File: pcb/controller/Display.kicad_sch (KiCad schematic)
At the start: 24 parts, among them J10 JST XH, J11 JST XH, J12 JST XH, J13 JST XH, J5 OLED 0.96" (I2C), J6 JST XH, J7 JST XH, J8 JST XH, J9 JST XH, Q2 SI2301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

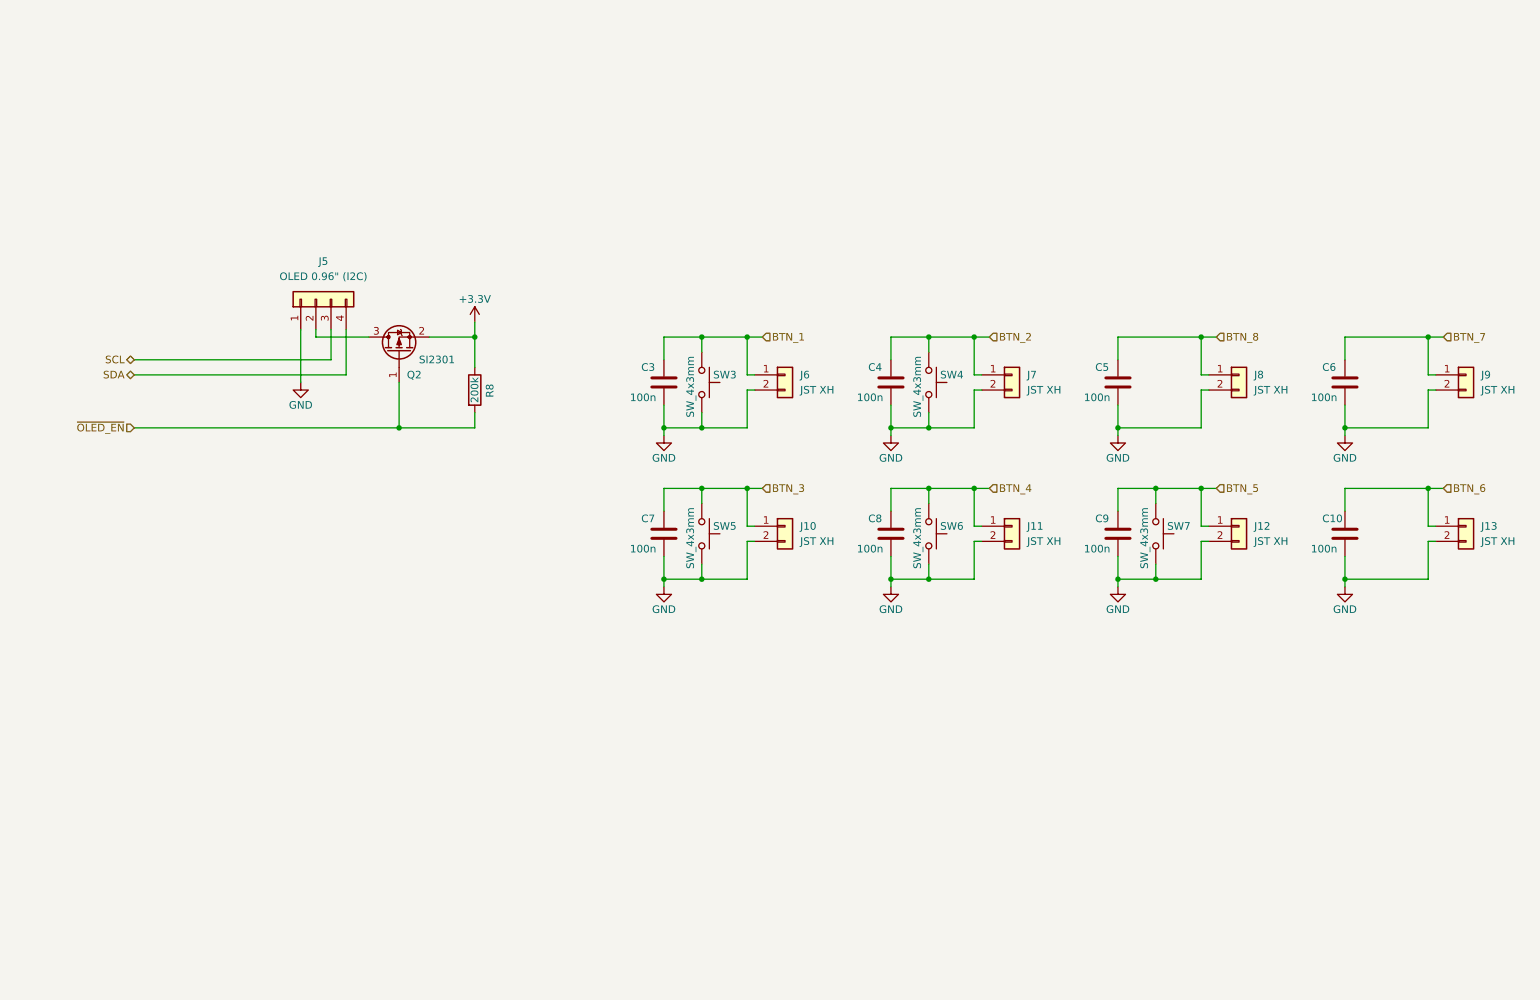
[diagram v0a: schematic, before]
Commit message: Revision 01 of Controller hardware
- fixed bugs from revision 00
- changed folder structure
- added ReleaseNotes_Controller.md to keep track of changes
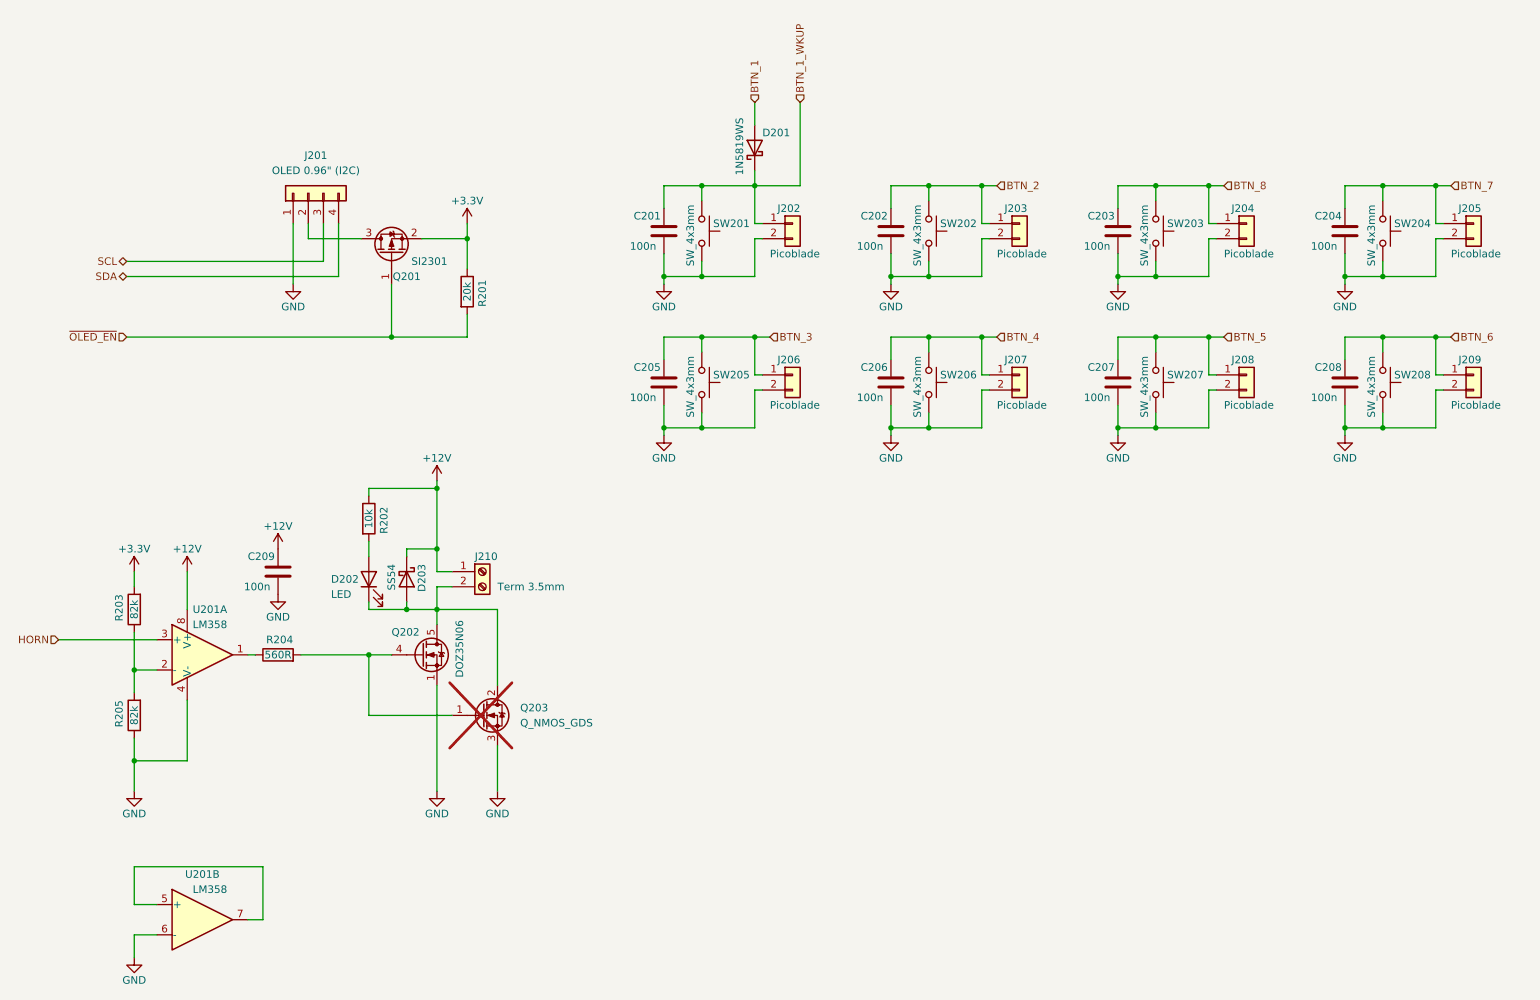
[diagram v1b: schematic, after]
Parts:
- added C209: 100n, Capacitor_SMD:C_0402_1005Metric, symbol Device:C
- added D201: 1N5819WS, Diode_SMD:D_SOD-323, symbol Diode:1N5819WS
- added D202: LED, LED_SMD:LED_0603_1608Metric, symbol Device:LED
- added D203: SS54, Diode_SMD:D_SMA, symbol Device:D_Schottky
- added J210: Term 3.5mm, Connector_Phoenix_MC:PhoenixContact_MC_1,5_2-G-3.5_1x02_P3.50mm_Horizontal, symbol Connector:Screw_Terminal_01x02
- added Q202: DOZ35N06, Package_SON:VSON-8_3.3x3.3mm_P0.65mm_NexFET, symbol Ravenspark:60N03D
- added Q203: Q_NMOS_GDS, Package_TO_SOT_SMD:TO-252-2, symbol Device:Q_NMOS_GDS
- added R202: 10k, Resistor_SMD:R_0402_1005Metric, symbol Device:R
- added R203, R205: 82k, Resistor_SMD:R_0402_1005Metric, symbol Device:R
- added R204: 560R, Resistor_SMD:R_0402_1005Metric, symbol Device:R
- added SW203, SW204, SW208: SW_4x3mm, RVNSPRK_Switch:SW_Push_4x3mm, symbol Switch:SW_Push
- added U201: LM358, Package_SO:SOIC-8_3.9x4.9mm_P1.27mm, symbol Amplifier_Operational:LM358
- C201: renamed from C3; LCSC Part # (none) -> C307331
- C202: renamed from C4; LCSC Part # (none) -> C307331
- C203: renamed from C5; LCSC Part # (none) -> C307331
- C204: renamed from C6; LCSC Part # (none) -> C307331
- C205: renamed from C7; LCSC Part # (none) -> C307331
- C206: renamed from C8; LCSC Part # (none) -> C307331
- C207: renamed from C9; LCSC Part # (none) -> C307331
- C208: renamed from C10; LCSC Part # (none) -> C307331
- J201: renamed from J5; footprint Connector_PinSocket_2.54mm:PinSocket_1x04_P2.54mm_Vertical -> Connector_PinSocket_2.54mm:PinSocket_1x04_P2.54mm_Vertical_SMD_Pin1Left; LCSC Part # (none) -> C20071191
- J202: renamed from J6; value JST XH -> Picoblade; LCSC Part # (none) -> C2845535
- J203: renamed from J7; value JST XH -> Picoblade; LCSC Part # (none) -> C2845535
- J204: renamed from J8; value JST XH -> Picoblade; LCSC Part # (none) -> C2845535
- J205: renamed from J9; value JST XH -> Picoblade; LCSC Part # (none) -> C2845535
- J206: renamed from J10; value JST XH -> Picoblade; LCSC Part # (none) -> C2845535
- J207: renamed from J11; value JST XH -> Picoblade; LCSC Part # (none) -> C2845535
- J208: renamed from J12; value JST XH -> Picoblade; LCSC Part # (none) -> C2845535
- J209: renamed from J13; value JST XH -> Picoblade; LCSC Part # (none) -> C2845535
- Q201: renamed from Q2; LCSC Part # (none) -> C10487
- R201: renamed from R8; value 200k -> 20k
- SW201: renamed from SW3; LCSC Part # (none) -> C18078117
- SW202: renamed from SW4; LCSC Part # (none) -> C18078117
- SW205: renamed from SW5; LCSC Part # (none) -> C18078117
- SW206: renamed from SW6; LCSC Part # (none) -> C18078117
- SW207: renamed from SW7; LCSC Part # (none) -> C18078117
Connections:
- net +3.3V: now also R203.2
- net BTN_1: now also D201.2 (A); no longer C201.1, J202.1 (Pin_1), SW201.1
- net BTN_6: now also SW208.1
- net BTN_7: now also SW204.1
- net BTN_8: now also SW203.1
- net GND: now also C209.2, Q202.1 (S), Q202.2 (S), Q202.3 (S), Q203.3 (S), R205.1, SW203.2, SW204.2, SW208.2, U201.4 (V-), U201.6 (-)
- new net: D202.2 (A), R202.2
- new net: Q202.4 (G), Q203.1 (G), R204.2
- new net: D202.1 (K), D203.2 (A), J210.2 (Pin_2), Q202.5 (D), Q203.2 (D)
- new net: U201.5 (+), U201.7
- new net: R204.1, U201.1
- new net: R203.1, R205.2, U201.2 (-)
- new net +12V: C209.1, D203.1 (K), J210.1 (Pin_1), R202.1, U201.8 (V+)
- new net BTN_1_WKUP: C201.1, D201.1 (K), J202.1 (Pin_1), SW201.1
- new net HORN: U201.3 (+)
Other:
- title: Display & Buttons -> Display, Buttons & Output
- moved on the sheet: C201, C202, C203, C204, C205, C206, C207, C208, J201, J202, J203, J204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

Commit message: Final adjustments and BOM optimization
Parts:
- R202: value 10k -> 1k
- R203, R205: value 82k -> 20k
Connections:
- net +12V: no longer R202.1
- net GND: now also D202.1 (K)
- net at Q202.4 (G), Q203.1 (G), R204.2: now also R202.1
- net at D203.2 (A), J210.2 (Pin_2), Q202.5 (D)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: no longer D202.1 (K)
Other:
- moved on the sheet: D202, R202
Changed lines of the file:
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@@
 	(title_block
 		(title "Display, Buttons & Output")
-		(date "2025-03-30")
+		(date "2025-04-09")
 		(rev "01")
 		(company "Ravenspark")
@@
 	)
 	(junction
-		(at 83.82 121.92)
-		(diameter 0)
-		(color 0 0 0 0)
-	)
-	(junction
 		(at 218.44 50.8)
 		(diameter 0)
@@
 	)
 	(junction
-		(at 209.55 50.8)
+		(at 69.85 129.54)
 		(diameter 0)
 		(color 0 0 0 0)
 	)
 	(junction
-		(at 209.55 66.04)
+		(at 209.55 50.8)
 		(diameter 0)
 		(color 0 0 0 0)
 	)
 	(junction
-		(at 88.9 101.6)
+		(at 209.55 66.04)
 		(diameter 0)
 		(color 0 0 0 0)
@@
 	(wire
 		(pts
-			(xy 77.47 121.92) (xy 83.82 121.92)
-		)
-		(stroke
-			(width 0)
-			(type default)
-		)
-	)
-	(wire
-		(pts
 			(xy 218.44 57.15) (xy 218.44 50.8)
 		)
@@
 	(wire
 		(pts
-			(xy 88.9 100.33) (xy 88.9 101.6)
+			(xy 88.9 100.33) (xy 88.9 111.76)
 		)
 		(stroke
@@
 	(wire
 		(pts
-			(xy 77.47 120.65) (xy 77.47 121.92)
+			(xy 69.85 148.59) (xy 69.85 152.4)
 		)
 		(stroke
@@
 	(wire
 		(pts
-			(xy 77.47 101.6) (xy 77.47 102.87)
+			(xy 69.85 129.54) (xy 69.85 130.81)
 		)
 		(stroke
@@
 	(wire
 		(pts
-			(xy 88.9 101.6) (xy 88.9 111.76)
-		)
-		(stroke
-			(width 0)
-			(type default)
-		)
-	)
-	(wire
-		(pts
 			(xy 142.24 36.83) (xy 142.24 40.64)
 		)
@@
 	(wire
 		(pts
-			(xy 77.47 110.49) (xy 77.47 113.03)
+			(xy 69.85 138.43) (xy 69.85 140.97)
 		)
 		(stroke
@@
 	(wire
 		(pts
-			(xy 66.04 129.54) (xy 77.47 129.54)
+			(xy 66.04 129.54) (xy 69.85 129.54)
 		)
 		(stroke
@@
 	(wire
 		(pts
-			(xy 77.47 101.6) (xy 88.9 101.6)
+			(xy 69.85 129.54) (xy 77.47 129.54)
 		)
 		(stroke
@@
 	(symbol
 		(lib_id "Device:R")
-		(at 77.47 106.68 0)
+		(at 69.85 134.62 0)
 		(unit 1)
 		(exclude_from_sim no)
@@
 		(dnp no)
 		(property "Reference" "R202"
-			(at 80.01 109.22 90)
+			(at 72.39 137.16 90)
 			(effects
 				(font
@@
 			)
 		)
-		(property "Value" "10k"
-			(at 77.47 106.68 90)
+		(property "Value" "1k"
+			(at 69.85 134.62 90)
 			(effects
 				(font
@@
 		)
 		(property "Footprint" "Resistor_SMD:R_0402_1005Metric"
-			(at 75.692 106.68 90)
+			(at 68.072 134.62 90)
 			(effects
 				(font
@@
 		)
 		(property "Datasheet" "~"
-			(at 77.47 106.68 0)
+			(at 69.85 134.62 0)
 			(effects
 				(font
@@
 		)
 		(property "Description" "Resistor"
-			(at 77.47 106.68 0)
+			(at 69.85 134.62 0)
 			(effects
 				(font
@@
 	(symbol
 		(lib_id "power:GND")
+		(at 69.85 152.4 0)
+		(unit 1)
+		(exclude_from_sim no)
+		(in_bom yes)
+		(on_board yes)
+		(dnp no)
+		(property "Reference" "#PWR0309"
+			(at 69.85 158.75 0)
+			(effects
+				(font
+					(size 1.27 1.27)
+				)
+				(hide yes)
+			)
+		)
+		(property "Value" "GND"
+			(at 69.85 156.21 0)
+			(effects
+				(font
+					(size 1.27 1.27)
+				)
+			)
+		)
+		(property "Footprint" ""
+			(at 69.85 152.4 0)
+			(effects
+				(font
+					(size 1.27 1.27)
+				)
+				(hide yes)
+			)
+		)
+		(property "Datasheet" ""
+			(at 69.85 152.4 0)
+			(effects
+				(font
+					(size 1.27 1.27)
+				)
+				(hide yes)
+			)
+		)
+		(property "Description" "Power symbol creates a global label with name \"GND\" , ground"
+			(at 69.85 152.4 0)
+			(effects
+				(font
+					(size 1.27 1.27)
+				)
+				(hide yes)
+			)
+		)
+		(pin "1"
+		)
+		(instances
+			(project "Controller"
+				(path "/909ae33d-387b-4690-b0aa-ba1ded8f44db/3558ebfc-0d2b-4045-8134-74237a6e1083"
+					(reference "#PWR0309")
+					(unit 1)
+				)
+			)
+		)
+	)
+	(symbol
+		(lib_id "power:GND")
 		(at 165.1 67.31 0)
 		(mirror y)
@@
 	(symbol
 		(lib_id "Device:LED")
-		(at 77.47 116.84 90)
+		(at 69.85 144.78 90)
 		(unit 1)
 		(exclude_from_sim no)
@@
 		(dnp no)
 		(property "Reference" "D202"
-			(at 71.12 116.84 90)
+			(at 63.5 144.78 90)
 			(effects
 				(font
@@
 		)
 		(property "Value" "LED"
-			(at 71.12 119.38 90)
+			(at 63.5 147.32 90)
 			(effects
 				(font
@@
 		)
 		(property "Footprint" "LED_SMD:LED_0603_1608Metric"
-			(at 77.47 116.84 0)
+			(at 69.85 144.78 0)
 			(effects
 				(font
@@
 		)
 		(property "Datasheet" "~"
-			(at 77.47 116.84 0)
+			(at 69.85 144.78 0)
 			(effects
 				(font
@@
 		)
 		(property "Description" "Light emitting diode"
-			(at 77.47 116.84 0)
+			(at 69.85 144.78 0)
 			(effects
 				(font
@@
 		)
 		(property "LCSC Part #" "C2286"
-			(at 77.47 116.84 0)
+			(at 69.85 144.78 0)
 			(effects
 				(font
@@
 			)
 		)
-		(property "Value" "82k"
+		(property "Value" "20k"
 			(at 38.1 121.92 90)
 			(effects
@@
 			)
 		)
-		(property "Value" "82k"
+		(property "Value" "20k"
 			(at 38.1 139.7 90)
 			(effects

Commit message: Updated ReleaseNotes_Controller.md with know issues of R01
Changed SMD button JLC order number to version without mounting holes
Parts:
- SW201, SW202, SW203, SW204, SW205, SW206, SW207, SW208: LCSC Part # C18078117 -> C18077679
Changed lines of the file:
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@@
 			)
 		)
-		(property "LCSC Part #" "C18078117"
+		(property "LCSC Part #" "C18077679"
 			(at 171.45 58.42 0)
 			(effects
@@
 			)
 		)
-		(property "LCSC Part #" "C18078117"
+		(property "LCSC Part #" "C18077679"
 			(at 209.55 58.42 0)
 			(effects
@@
 			)
 		)
-		(property "LCSC Part #" "C18078117"
+		(property "LCSC Part #" "C18077679"
 			(at 247.65 58.42 0)
 			(effects
@@
 			)
 		)
-		(property "LCSC Part #" "C18078117"
+		(property "LCSC Part #" "C18077679"
 			(at 133.35 83.82 0)
 			(effects
@@
 			)
 		)
-		(property "LCSC Part #" "C18078117"
+		(property "LCSC Part #" "C18077679"
 			(at 209.55 83.82 0)
 			(effects
@@
 			)
 		)
-		(property "LCSC Part #" "C18078117"
+		(property "LCSC Part #" "C18077679"
 			(at 247.65 83.82 0)
 			(effects
@@
 			)
 		)
-		(property "LCSC Part #" "C18078117"
+		(property "LCSC Part #" "C18077679"
 			(at 133.35 58.42 0)
 			(effects
@@
 			)
 		)
-		(property "LCSC Part #" "C18078117"
+		(property "LCSC Part #" "C18077679"
 			(at 171.45 83.82 0)
 			(effects
